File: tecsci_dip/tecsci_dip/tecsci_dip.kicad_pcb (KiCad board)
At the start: 2 copper layers, 76 x 60 mm, 40 parts, among them IC201 TMC5130, J201 Conn_01x19_ESP32, J202 Conn_01x19_ESP32, U201 AKL182_04_POL_HEADER, U301 Regulador_LM5161

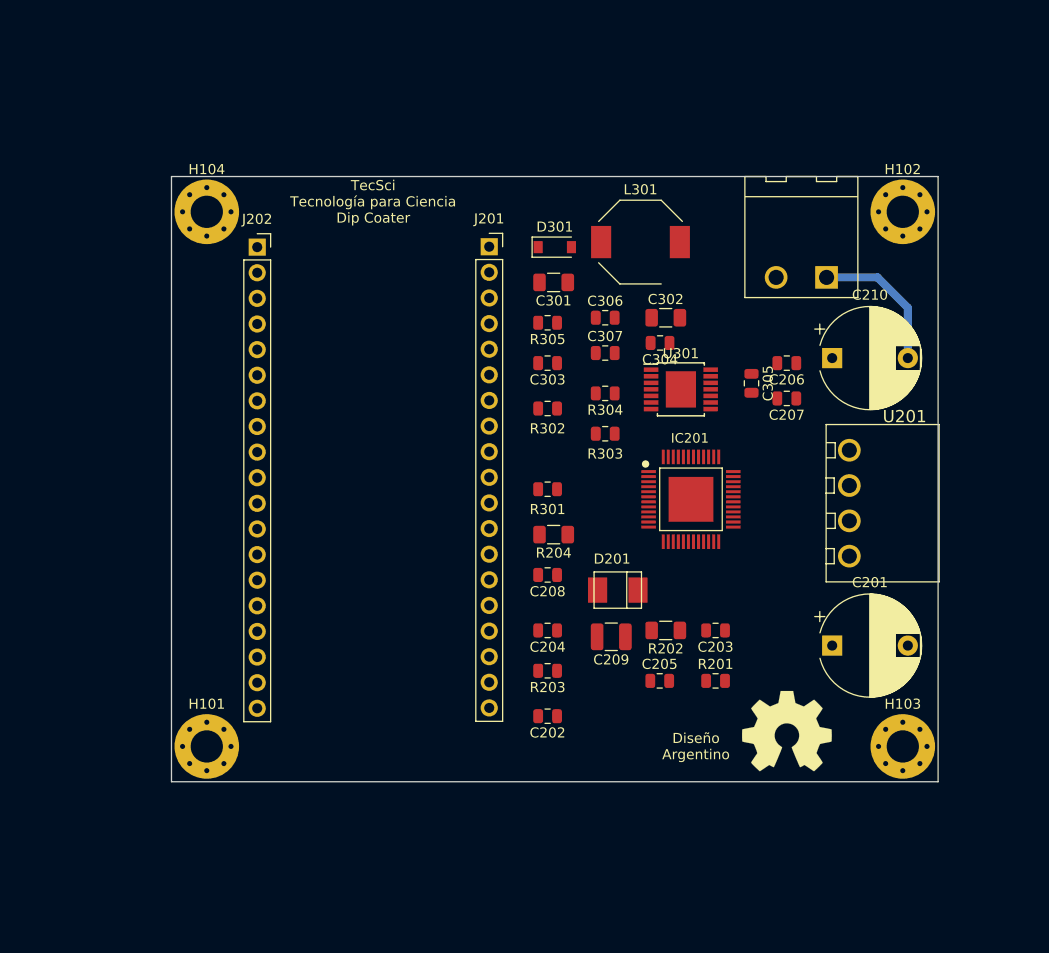
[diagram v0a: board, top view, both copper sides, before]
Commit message: add area de cobre
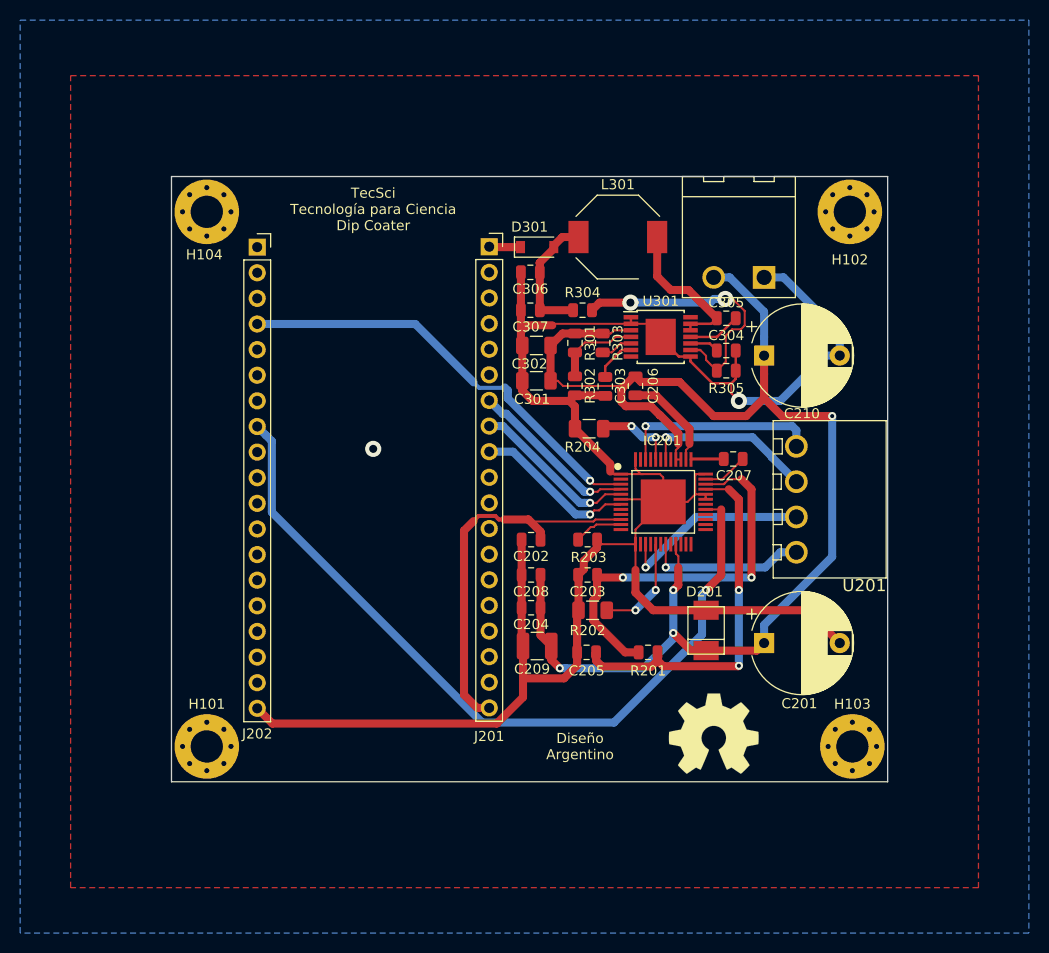
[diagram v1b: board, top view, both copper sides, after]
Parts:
- moved R305 18.3 mm to (105.0, 74.2), turned to 0 degrees
- moved C202 17.6 mm to (85.7, 91.0)
- moved C206 15.2 mm to (96.0, 75.8), turned to 270 degrees
- moved R301 14.8 mm to (90.0, 71.5), turned to 90 degrees
- moved C203 13.8 mm to (91.2, 94.5)
- moved R203 13.6 mm to (91.2, 91.0), turned to 0 degrees
- moved C302 13.1 mm to (86.2, 71.8), turned to 180 degrees
- moved R204 11.1 mm to (91.4, 80.0)
- moved C301 9.90 mm to (86.2, 75.2)
- moved D201 9.63 mm to (103.0, 100.0), turned to 90 degrees
- moved R303 9.00 mm to (92.8, 71.5), turned to 90 degrees
- moved C306 8.68 mm to (85.6, 64.5), turned to 180 degrees
- moved R304 8.55 mm to (90.8, 68.2), turned to 0 degrees
- moved C307 8.55 mm to (85.6, 68.2), turned to 180 degrees
- moved C207 8.01 mm to (105.7, 83.0)
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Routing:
- net GND: track 14.3 -> 202.8 mm, vias 0 -> 2
- net +24V: track 0.00 -> 137.9 mm, vias 0 -> 4
- net /esp32_tmc5130_/DRV_ENA: track 0.00 -> 78.7 mm, vias 0 -> 1
- net /esp32_tmc5130_/CSN: track 0.00 -> 43.5 mm, vias 0 -> 1
- net Net-(C203-Pad1): track 0.00 -> 39.8 mm, vias 0 -> 2
- net +3V3: track 0.00 -> 38.3 mm
- net Net-(C205-Pad2): track 0.00 -> 36.7 mm, vias 0 -> 2
- net Net-(R304-Pad2): track 0.00 -> 27.4 mm, vias 0 -> 2
- net Net-(IC201-Pad46): track 0.00 -> 20.0 mm, vias 0 -> 1
- net Net-(IC201-Pad15): track 0.00 -> 19.3 mm, vias 0 -> 1
- net Net-(IC201-Pad42): track 0.00 -> 17.0 mm, vias 0 -> 1
- net /esp32_tmc5130_/SCK: track 0.00 -> 16.9 mm, vias 0 -> 1
- net /esp32_tmc5130_/MOSI: track 0.00 -> 16.6 mm, vias 0 -> 1
- net /esp32_tmc5130_/MISO: track 0.00 -> 16.0 mm, vias 0 -> 1
- net Net-(IC201-Pad19): track 0.00 -> 15.9 mm, vias 0 -> 1
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- added copper zone on B.Cu, net GND
- added copper zone on F.Cu, net GND
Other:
- board size 76 x 60 mm -> 71 x 60 mm
- board text added: "Grilla de posicionamiento: Principal 0,5mm Alternativa 0,25mm Grilla de ruteo: Principal 0,5mm Alternativa 0,25mm Pistas: Principal 0.8mm Alternativa 0.2mm (Límite Mayer 8mils - 0.20mm) Vías: Principal 1.6mm/0.8mm Alternativa 0.8mm/0.4mm (Límite Mayer 8mils - 0.80mm) Margen General : 0,3 mm Margen Particular: 0,2 mm Componentes -> 201 301 (Límite Mayer 8mils - 0.18mm) Base para las restricciones 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"
- board text removed: "Grilla de posicionamiento: Principal 0,5mm Grilla de ruteo: Principal 0,5mm Alternativa 0,25mm Pistas: Principal 0.3mm Alternativa 1.5mm Vías: Principal 1.6mm/0.8mm Margen General : 0,8 mm Margen Particular: 0,2 mm Componentes -> 201 301 Base para las restricciones Ernesto Mayer, Estandar 10 mils"

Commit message: add fiduciales
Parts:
- added FID101: Fiducial, Fiducial:Fiducial_1mm_Mask2mm, F.Cu at (65.0, 66.5)
- added FID102: Fiducial, Fiducial:Fiducial_1mm_Mask2mm, F.Cu at (118.0, 66.5)
- added FID103: Fiducial, Fiducial:Fiducial_1mm_Mask2mm, F.Cu at (65.0, 106.0)

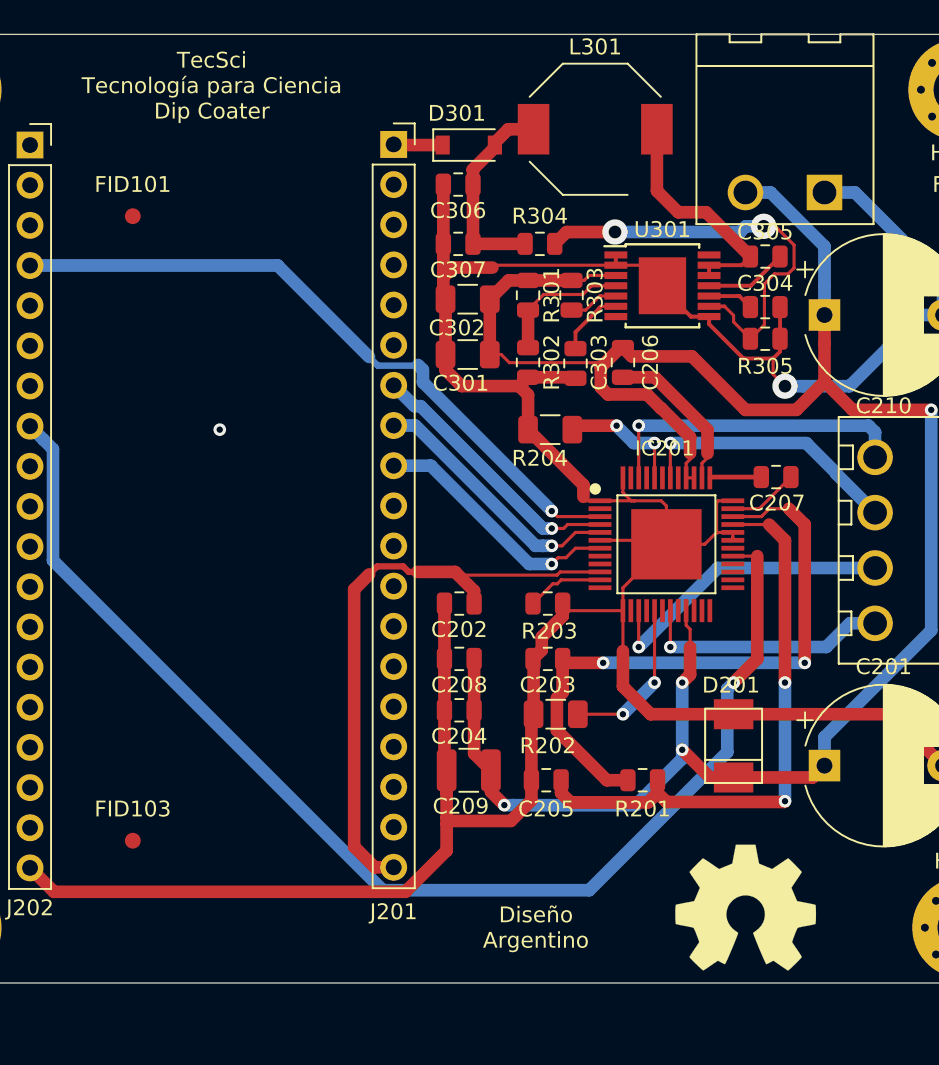
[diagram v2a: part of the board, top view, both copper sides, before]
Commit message: add license CERN OHL v.1.2
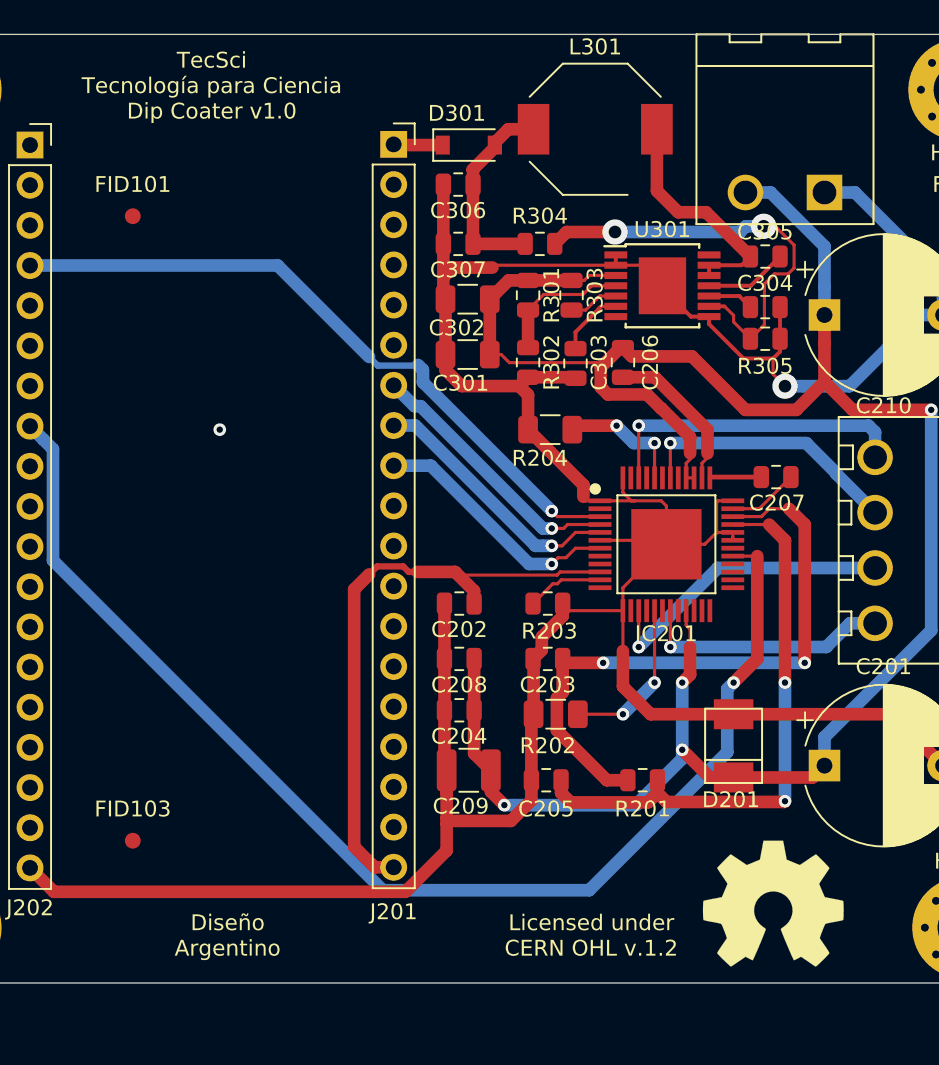
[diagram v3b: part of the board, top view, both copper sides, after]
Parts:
- moved OSHWA101 1.77 mm to (105.5, 110.0)
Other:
- board text added: "Licensed under CERN OHL v.1.2"
- board text added: "TecSci Tecnología para Ciencia Dip Coater v1.0"
- board text removed: "TecSci Tecnología para Ciencia Dip Coater"
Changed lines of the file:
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@@
   )
   (page A4)
+  (title_block
+    (title "Dip Coater")
+    (date 2019-10-28)
+    (rev 1)
+    (company "Tecsci Tecnología para Ciencia")
+    (comment 1 "Diseñador :Martin Abel Gambarotta")
+    (comment 2 "Revisor: Mariano Campos")
+  )
   (layers
     (0 F.Cu signal)
@@
   )
   (module Symbol:OSHW-Symbol_8.9x8mm_SilkScreen (layer F.Cu)
-    (at 103.75 110.25)
+    (at 105.5 110)
     (descr "Open Source Hardware Symbol")
     (tags "Logo Symbol OSHW")
@@
     (at 98.75 87.25)
     (clearance 0.2)
-    (fp_text reference IC201 (at -2 -5.5) (layer F.SilkS)
-      (effects (font (size 0.95 0.95) (thickness 0.1)) (justify left bottom))
+    (fp_text reference IC201 (at -2 6.25) (layer F.SilkS)
+      (effects (font (size 1 1) (thickness 0.15)) (justify left bottom))
     )
     (fp_text value TMC5130 (at -3 0.5) (layer F.Fab)
@@
   (module TMC5130-Eval_v15:SMB (layer F.Cu)
     (at 103 100 90)
-    (fp_text reference D201 (at 3.25 -2) (layer F.SilkS)
+    (fp_text reference D201 (at -4 -2) (layer F.SilkS)
       (effects (font (size 1 1) (thickness 0.15)) (justify left bottom))
     )
@@
     )
   )
+  (gr_text "Licensed under \nCERN OHL v.1.2" (at 94 112) (layer F.SilkS)
+    (effects (font (size 1 1) (thickness 0.15)))
+  )
   (dimension 71 (width 0.12) (layer F.SilkS)
     (gr_text "71,000 mm" (at 85.5 47.73) (layer F.SilkS)
@@
   (gr_line (start 121 115) (end 121 55) (layer Edge.Cuts) (width 0.05))
   (gr_line (start 50 115) (end 121 115) (layer Edge.Cuts) (width 0.05))
-  (gr_text "TecSci\nTecnología para Ciencia\nDip Coater" (at 70 58.25) (layer F.SilkS)
+  (gr_text "TecSci\nTecnología para Ciencia\nDip Coater v1.0" (at 70 58.25) (layer F.SilkS)
     (effects (font (size 1 1) (thickness 0.15)))
   )
-  (gr_text "Diseño \nArgentino" (at 90.5 111.5) (layer F.SilkS)
+  (gr_text "Diseño \nArgentino" (at 71 112) (layer F.SilkS)
     (effects (font (size 1 1) (thickness 0.15)))
   )
@@
     (arrow2b (pts (xy 46.25 62) (xy 46.836421 63.126504)))
   )
-  (dimension 23 (width 0.12) (layer F.SilkS)
-    (gr_text "23,000 mm" (at 70 110.73) (layer F.SilkS)
-      (effects (font (size 1 1) (thickness 0.15)))
-    )
-    (feature1 (pts (xy 81.5 112.249999) (xy 81.5 111.413579)))
-    (feature2 (pts (xy 58.5 112.249999) (xy 58.5 111.413579)))
-    (crossbar (pts (xy 58.5 112) (xy 81.5 112)))
-    (arrow1a (pts (xy 81.5 112) (xy 80.373496 112.586421)))
-    (arrow1b (pts (xy 81.5 112) (xy 80.373496 111.413579)))
-    (arrow2a (pts (xy 58.5 112) (xy 59.626504 112.586421)))
-    (arrow2b (pts (xy 58.5 112) (xy 59.626504 111.413579)))
-  )
   (segment (start 84.6425 64.5) (end 84.6425 68.25) (width 0.8) (layer F.Cu) (net 1))

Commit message: add correcciones compañero
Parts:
- moved H101 11.5 mm to (65.0, 111.2)
- moved H104 11.5 mm to (65.0, 58.8)
- moved FID103 1.00 mm to (65.0, 105.0)
- moved H103 0.35 mm to (117.2, 111.2)
- moved H102 0.25 mm to (117.2, 58.8)
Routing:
- net /esp32_tmc5130_/DRV_ENA: track 78.7 -> 82.0 mm
- net Net-(IC201-Pad46): track 20.0 -> 23.0 mm
- net Net-(IC201-Pad42): track 17.0 -> 16.1 mm
- net Net-(C205-Pad2): track 36.7 -> 37.5 mm
- net Net-(IC201-Pad19): track 15.9 -> 15.1 mm
- net Net-(IC201-Pad15): track 19.3 -> 19.9 mm
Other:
- board size 71 x 60 mm -> 65 x 60 mm
- board text added: "Grilla de posicionamiento: Principal 0,5mm Alternativa 0,25mm Grilla de ruteo: Principal 0,5mm Alternativa 0,25mm Mounting Hole: Principal: 3,2mm Pistas: Principal 0.8mm Alternativa inferior 0.2mm (Límite Mayer 8mils - 0.20mm) Alternativa superior 2mm Vías: Principal 1.6mm/0.8mm Alternativa 0.8mm/0.4mm (Límite Mayer 8mils - 0.80mm) Margen General : 0,3 mm Margen Particular: 0,2 mm Componentes -> 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"
- board text added: "TECSCI"
- board text added: "https://tecsci.com.ar/"
- board text removed: "Grilla de posicionamiento: Principal 0,5mm Alternativa 0,25mm Grilla de ruteo: Principal 0,5mm Alternativa 0,25mm Pistas: Principal 0.8mm Alternativa 0.2mm (Límite Mayer 8mils - 0.20mm) Vías: Principal 1.6mm/0.8mm Alternativa 0.8mm/0.4mm (Límite Mayer 8mils - 0.80mm) Margen General : 0,3 mm Margen Particular: 0,2 mm Componentes -> 201 301 (Límite Mayer 8mils - 0.18mm) Base para las restricciones 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"

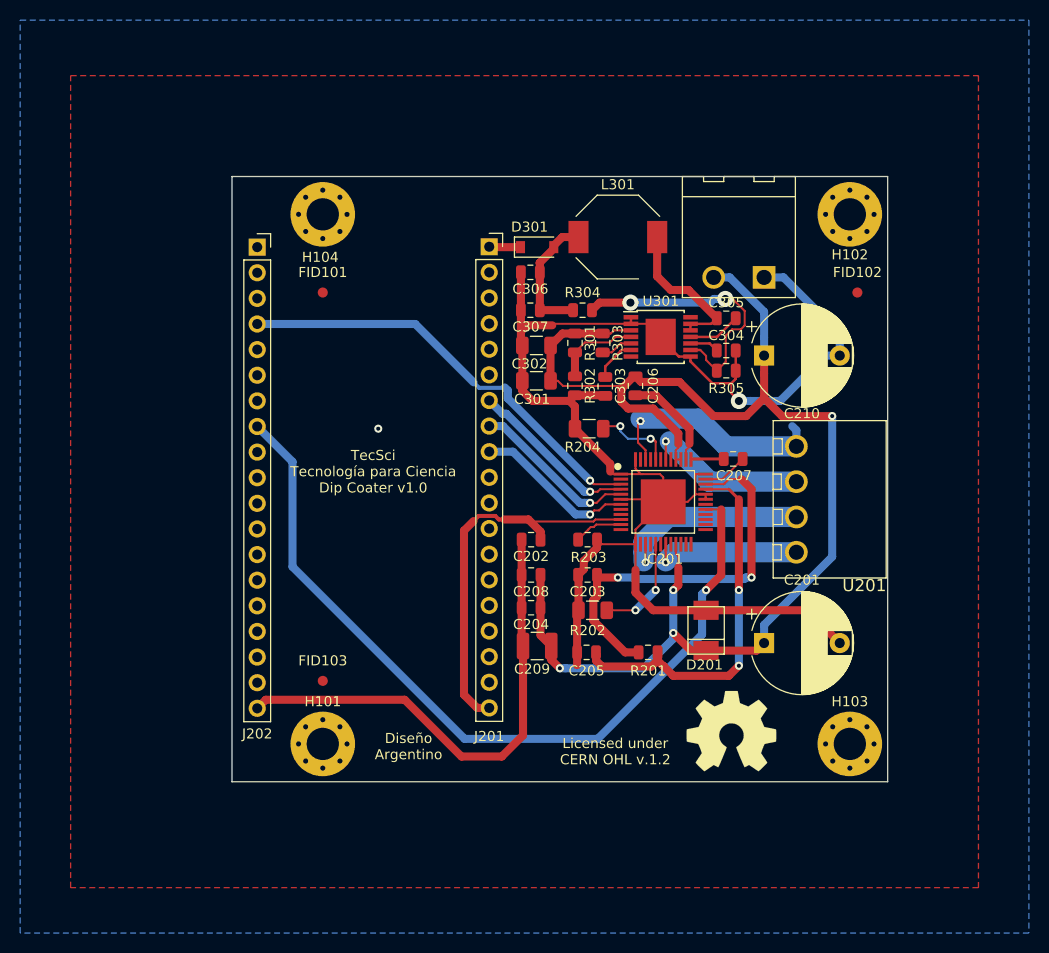
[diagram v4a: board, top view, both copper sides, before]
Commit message: Se corrigen todos los errores marcados por el profesor, excepto pasar a footprint conectores de ESP32, ya que la v2 contendra al CI
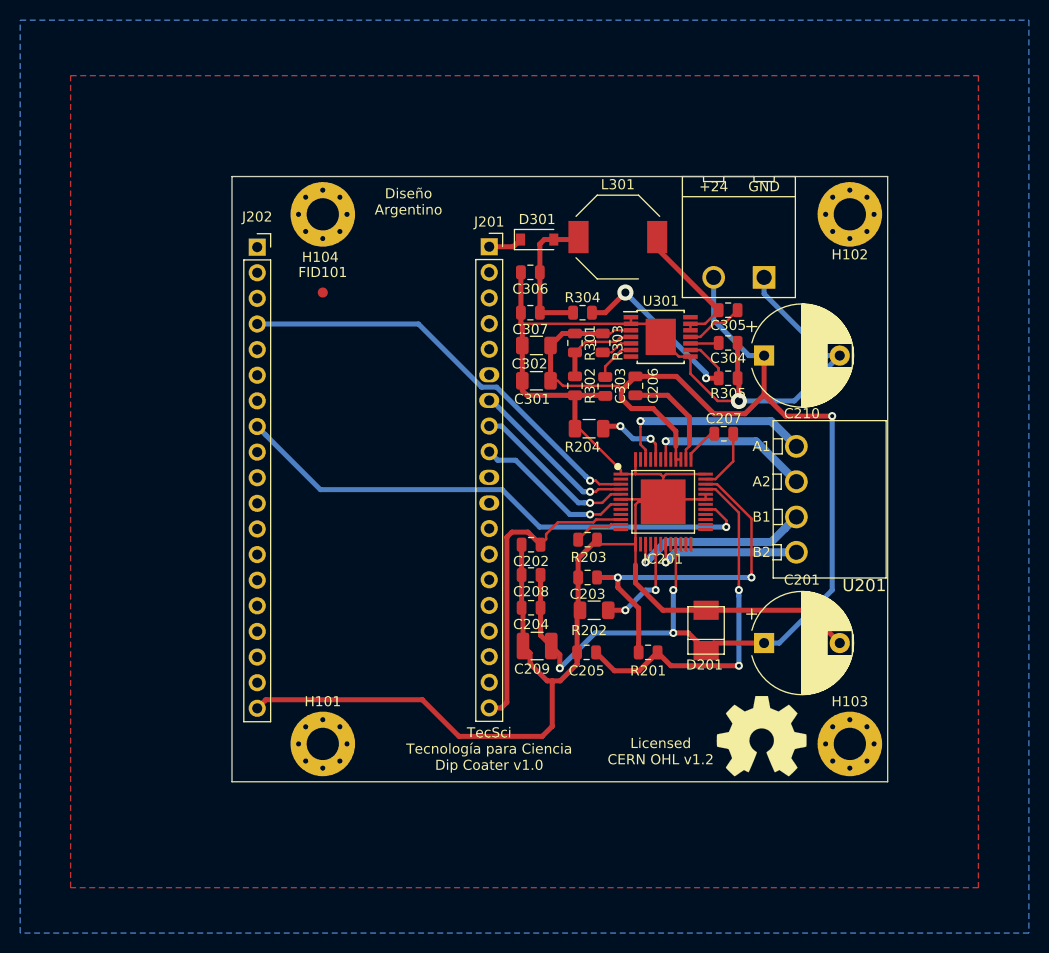
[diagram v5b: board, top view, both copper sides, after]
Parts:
- removed FID102, FID103: Fiducial, Fiducial:Fiducial_1mm_Mask2mm
- moved OSHWA101 3.04 mm to (108.5, 110.5)
- moved C207 2.67 mm to (104.8, 80.5)
- moved C305 0.82 mm to (105.2, 68.2)
- moved C304 0.77 mm to (105.2, 71.5)
- moved R305 0.77 mm to (105.2, 75.0)
- moved D301 0.75 mm to (86.2, 61.2)
- moved C202 0.50 mm to (85.7, 91.5)
- moved C203 0.25 mm to (91.2, 94.8)
- moved C307 0.25 mm to (85.6, 68.5)
- moved R304 0.25 mm to (90.8, 68.5)
- moved R202 0.15 mm to (91.9, 98.0)
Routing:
- net /esp32_tmc5130_/DRV_ENA: track 82.0 -> 53.8 mm
- net GND: track 202.5 -> 211.6 mm, vias 2 -> 1
- net +3V3: track 38.3 -> 31.7 mm
- net Net-(R304-Pad2): track 27.4 -> 21.7 mm
- net Net-(C203-Pad1): track 39.9 -> 35.4 mm
- net Net-(IC201-Pad46): track 23.0 -> 20.5 mm
- net Net-(C205-Pad2): track 37.5 -> 35.7 mm
- net Net-(C207-Pad1): track 4.50 -> 6.21 mm
- net Net-(IC201-Pad15): track 19.9 -> 18.6 mm
- net Net-(C305-Pad1): track 15.0 -> 13.8 mm
- net Net-(C306-Pad1): track 13.1 -> 14.0 mm
- net /esp32_tmc5130_/CSN: track 43.5 -> 42.6 mm
- net Net-(C206-Pad2): track 9.91 -> 10.6 mm
- net Net-(C305-Pad2): track 5.25 -> 5.77 mm
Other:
- net class Default: clearance 0.2 -> 0.22
- rule trace_clearance: 0.2 -> 0.22
- board text added: "+24"
- board text added: "A1"
- board text added: "A2"
- board text added: "B1"
- board text added: "B2"
- board text added: "GND"
- board text added: "Grilla de posicionamiento: Principal 0,25mm Grilla de ruteo: Principal 0,25mm Mounting Hole: Principal: 3,2mm Pistas: Principal 0.5mm Alternativa inferior 0.25mm (Límite Mayer 8mils - 0.20mm) Alternativa superior 0,8mm Vías: Principal 1.6mm/0.8mm Alternativa 0.8mm/0.4mm (Límite Mayer 8mils - 0.80mm) Margen General : 0,22 mm Margen Particular: 0,2 mm Componentes -> 201 301 (Límite Mayer 8mils - 0.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"
- board text added: "Licensed CERN OHL v1.2"
- board text removed: "Grilla de posicionamiento: Principal 0,5mm Alternativa 0,25mm Grilla de ruteo: Principal 0,5mm Alternativa 0,25mm Mounting Hole: Principal: 3,2mm Pistas: Principal 0.8mm Alternativa inferior 0.2mm (Límite Mayer 8mils - 0.20mm) Alternativa superior 2mm Vías: Principal 1.6mm/0.8mm Alternativa 0.8mm/0.4mm (Límite Mayer 8mils - 0.80mm) Margen General : 0,3 mm Margen Particular: 0,2 mm Componentes -> 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"
- board text removed: "Licensed under CERN OHL v.1.2"
